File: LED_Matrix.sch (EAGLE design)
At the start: 35 parts, among them IC1 KF33, IC2 FT232RL, Q1 16MHz, U1 HC_05

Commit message: version 1
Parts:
- removed JP2: (no value), pinhead:PINHD-1X2/90
- added C15: 100n, rcl:C-EUC0805
- added C16: 47n, rcl:C-EUC0805
- added C17: 10u, rcl:C-EUC0805
- added C18: 250u, rcl:CPOL-EU153CLV-0605
- added C19: 470n, rcl:C-EUC0805
- added J1: DCJ0202, con-jack:DCJ0202
- added LED3: (no value), led:LEDSML0805
- added LM386: LM386SO08, debegr92:LM386SO08
- added MIC: MIC_EMY-9765PEMY-9765P, debegr92:MIC_EMY-9765PEMY-9765P
- added Q2: (no value), semicon-smd-ipc:NPN-TRANSISTOR_SOT23
- added R6: 10, rcl:R-EU_R0805
- added R7: 10k, rcl:R-EU_R0805
- added R9: 470, rcl:R-EU_R0805
- added TRIMMER: 10k, Tobias:75H_RTRIM
- Q1: device special:XTAL -> crystal:CRYSTALHC49UP
- R8: value 10k -> 470
- renumbered 470 to R8, IC2 to FT232, JP1 to BTM, S2 to RESET, SJ1 to JTX, SJ2 to JRX, U$1 to USB, U1 to HC05
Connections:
- new net BTM_RST: ATMEGA328.PB0(ICP1/CLKO/PCINT0), R7.1
- new net N$16: C19.1, MIC.1, TRIMMER.S
- new net N$17: C17.2, LM386.GAIN2
- new net N$18: C16.2, R6.1
- new net N$2: C15.1, LM386.BYPASS
- new net N$20: C17.1, LM386.GAIN1
- new net N$21: C16.1, C18.+, LM386.OUT
- new net N$22: C19.2, LM386.+
- new net N$23: C9.1, HC05.RST, Q2.C, R5.2
- new net N$24: HC05.PIO1, LED3.A
- new net N$25: LED3.C, R9.2
- net +5V: now also J1.1, LM386.V+, TRIMMER.E; no longer JP2.2
- net AUDIO_IN: now also C18.-
- net GND: now also C15.2, HC05.GND2, J1.2, J1.3, LM386.-, LM386.GND, MIC.2, Q2.E, R6.2, R9.1, TRIMMER.A; no longer JP2.1
- net N$12: now also ATMEGA328.PC3(ADC3/PCINT11)
- net N$15: now also ATMEGA328.PC2(ADC2/PCINT10)
- net N$19: now also Q2.B, R7.2; no longer C9.1, HC05.RST, R5.2
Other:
- note added: "Gain 200"
- moved on the sheet: C1, C10, C2, C8, C9, ISP, MATRIX, R2, R5

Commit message: analog switch added
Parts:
- removed BTM: (no value), jumper:JP2W
- added Q3: (no value), semicon-smd-ipc:NPN-TRANSISTOR_SOT23
- added R10: 1k, rcl:R-EU_R0805
- R7: value 10k -> 1k
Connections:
- removed net N$10: BTM.1, R4.2
- new net N$27: Q3.B, R10.2
- net BTM_MODESELECT: now also Q3.C, R10.1, R4.2; no longer BTM.2
- net GND: now also Q3.E; no longer BTM.3
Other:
- moved on the sheet: R4
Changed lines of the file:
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@@
 <part name="R3" library="rcl" deviceset="R-EU_" device="R0805" value="470"/>
 <part name="GND8" library="supply1" deviceset="GND" device=""/>
-<part name="BTM" library="jumper" deviceset="JP2W" device=""/>
-<part name="GND9" library="supply1" deviceset="GND" device=""/>
 <part name="R4" library="rcl" deviceset="R-EU_" device="R0805" value="10k"/>
 <part name="P+8" library="supply1" deviceset="+5V" device=""/>
@@
 <part name="Q2" library="semicon-smd-ipc" deviceset="NPN-TRANSISTOR_" device="SOT23"/>
 <part name="GND18" library="supply1" deviceset="GND" device=""/>
-<part name="R7" library="rcl" deviceset="R-EU_" device="R0805" value="10k"/>
+<part name="R7" library="rcl" deviceset="R-EU_" device="R0805" value="1k"/>
 <part name="LED3" library="led" deviceset="LED" device="SML0805"/>
 <part name="GND19" library="supply1" deviceset="GND" device=""/>
 <part name="R8" library="rcl" deviceset="R-EU_" device="R0805" value="470"/>
 <part name="R9" library="rcl" deviceset="R-EU_" device="R0805" value="470"/>
+<part name="Q3" library="semicon-smd-ipc" deviceset="NPN-TRANSISTOR_" device="SOT23"/>
+<part name="R10" library="rcl" deviceset="R-EU_" device="R0805" value="1k"/>
+<part name="GND9" library="supply1" deviceset="GND" device=""/>
 </parts>
 <sheets>
@@
 <instance part="R3" gate="G$1" x="121.92" y="45.72" rot="R90"/>
 <instance part="GND8" gate="1" x="121.92" y="30.48"/>
-<instance part="BTM" gate="1" x="137.16" y="55.88" rot="R270"/>
-<instance part="GND9" gate="1" x="129.54" y="48.26"/>
-<instance part="R4" gate="G$1" x="132.08" y="66.04" rot="R270"/>
+<instance part="R4" gate="G$1" x="127" y="63.5" rot="R270"/>
 <instance part="P+8" gate="1" x="187.96" y="132.08"/>
 <instance part="GND10" gate="1" x="187.96" y="66.04"/>
@@
 <instance part="P+6" gate="1" x="185.42" y="58.42"/>
 <instance part="+3V3" gate="G$1" x="231.14" y="58.42"/>
-<instance part="+3V4" gate="G$1" x="132.08" y="76.2"/>
+<instance part="+3V4" gate="G$1" x="127" y="73.66"/>
 <instance part="USB" gate="G$1" x="172.72" y="93.98"/>
 <instance part="P+7" gate="1" x="180.34" y="101.6"/>
@@
 <instance part="R8" gate="G$1" x="116.84" y="43.18" rot="R90"/>
 <instance part="R9" gate="G$1" x="111.76" y="25.4" rot="R90"/>
+<instance part="Q3" gate="G$1" x="129.54" y="48.26" rot="MR0"/>
+<instance part="R10" gate="G$1" x="137.16" y="43.18" rot="R90"/>
+<instance part="GND9" gate="1" x="127" y="38.1"/>
 </instances>
 <busses>
@@
 <junction x="121.92" y="35.56"/>
 <pinref part="R8" gate="G$1" pin="1"/>
-</segment>
-<segment>
-<pinref part="GND9" gate="1" pin="GND"/>
-<pinref part="BTM" gate="1" pin="3"/>
-<wire x1="129.54" y1="50.8" x2="129.54" y2="53.34" width="0.1524" layer="91"/>
-<wire x1="129.54" y1="53.34" x2="134.62" y2="53.34" width="0.1524" layer="91"/>
 </segment>
 <segment>
@@
 <pinref part="R9" gate="G$1" pin="1"/>
 </segment>
+<segment>
+<pinref part="Q3" gate="G$1" pin="E"/>
+<pinref part="GND9" gate="1" pin="GND"/>
+<wire x1="127" y1="43.18" x2="127" y2="40.64" width="0.1524" layer="91"/>
+</segment>
 </net>
 <net name="N$7" class="0">
@@
 <net name="BTM_MODESELECT" class="0">
 <segment>
-<pinref part="BTM" gate="1" pin="2"/>
 <pinref part="HC05" gate="G$1" pin="PIO11"/>
-<wire x1="134.62" y1="55.88" x2="119.38" y2="55.88" width="0.1524" layer="91"/>
-<wire x1="119.38" y1="55.88" x2="96.52" y2="55.88" width="0.1524" layer="91"/>
-<wire x1="119.38" y1="55.88" x2="119.38" y2="63.5" width="0.1524" layer="91"/>
-<wire x1="119.38" y1="63.5" x2="114.3" y2="63.5" width="0.1524" layer="91"/>
-<junction x="119.38" y="55.88"/>
-<label x="114.3" y="63.5" size="1.27" layer="95" rot="R180" xref="yes"/>
+<wire x1="127" y1="55.88" x2="96.52" y2="55.88" width="0.1524" layer="91"/>
+<wire x1="127" y1="53.34" x2="127" y2="55.88" width="0.1524" layer="91"/>
+<pinref part="R4" gate="G$1" pin="2"/>
+<wire x1="127" y1="55.88" x2="127" y2="58.42" width="0.1524" layer="91"/>
+<junction x="127" y="55.88"/>
+<pinref part="Q3" gate="G$1" pin="C"/>
 </segment>
 <segment>
@@
 <label x="111.76" y="83.82" size="1.27" layer="95" xref="yes"/>
 </segment>
-</net>
-<net name="N$10" class="0">
-<segment>
-<pinref part="BTM" gate="1" pin="1"/>
-<wire x1="134.62" y1="58.42" x2="132.08" y2="58.42" width="0.1524" layer="91"/>
-<wire x1="132.08" y1="58.42" x2="132.08" y2="60.96" width="0.1524" layer="91"/>
-<pinref part="R4" gate="G$1" pin="2"/>
+<segment>
+<pinref part="R10" gate="G$1" pin="1"/>
+<wire x1="137.16" y1="38.1" x2="137.16" y2="35.56" width="0.1524" layer="91"/>
+<label x="137.16" y="35.56" size="1.27" layer="95" rot="R270" xref="yes"/>
 </segment>
 </net>
@@
 <segment>
 <pinref part="R4" gate="G$1" pin="1"/>
-<wire x1="132.08" y1="71.12" x2="132.08" y2="73.66" width="0.1524" layer="91"/>
+<wire x1="127" y1="68.58" x2="127" y2="71.12" width="0.1524" layer="91"/>
 <pinref part="+3V4" gate="G$1" pin="+3V3"/>
 </segment>
@@
 </segment>
 </net>
+<net name="N$27" class="0">
+<segment>
+<pinref part="R10" gate="G$1" pin="2"/>
+<pinref part="Q3" gate="G$1" pin="B"/>
+<wire x1="137.16" y1="48.26" x2="132.08" y2="48.26" width="0.1524" layer="91"/>
+</segment>
+</net>

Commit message: return point
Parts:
- removed JRX, JTX: (no value), jumper:SJ2W
- added LEDON: (no value), led:LEDSML0805
- added R11, R12, R13: 470, rcl:R-EU_R0805
- added U$1: DG2016, Tobias:DG2016
- C18: device rcl:CPOL-EU153CLV-0605 -> rcl:CPOL-EUE2.5-7
- MATRIX: device pinhead:PINHD-1X3/90 -> pinhead:PINHD-1X3
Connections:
- new net N$10: LEDON.C, R11.2
- new net N$26: HC05.RX, R12.1, R13.2
- new net N$28: ATMEGA328.PD2(INT0/PCINT18), U$1.IN1
- new net N$29: ATMEGA328.PD3(INT1/OC2B/PCINT19), U$1.IN2
- net +5V: now also LEDON.A, U$1.VCC
- net GND: now also R11.1, R13.1, U$1.GND
- net N$12: now also U$1.COM1; no longer JTX.2
- net N$15: now also U$1.COM2; no longer JRX.2
- net RX_BTM: now also R12.2, U$1.NC1; no longer HC05.RX, JRX.1
- net RX_FT232: now also U$1.NO1; no longer JRX.3
- net TX_BTM: now also U$1.NC2; no longer JTX.1
- net TX_FT232: now also U$1.NO2; no longer JTX.3

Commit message: version 2 Final
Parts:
- removed C15: 100n, rcl:C-EUC0805
- removed C16: 47n, rcl:C-EUC0805
- removed C17: 10u, rcl:C-EUC0805
- removed C18: 250u, rcl:CPOL-EUE2.5-7
- removed C19: 470n, rcl:C-EUC0805
- removed C4, C5: 22p, rcl:C-EUC0805
- removed LM386: LM386SO08, debegr92:LM386SO08
- removed MIC: MIC_EMY-9765PEMY-9765P, debegr92:MIC_EMY-9765PEMY-9765P
- removed Q1: 16MHz, crystal:CRYSTALHC49UP
- removed R6: 10, rcl:R-EU_R0805
- removed TRIMMER: 10k, Tobias:75H_RTRIM
- added Q4: CSTCR6M00G53Z, murata-filter:CSTCR6M00G53Z
- added SJ1: (no value), jumper:SJ
- renumbered IC1 to KF33, LEDON to D1, MATRIX to MTX, U$1 to DG2016
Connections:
- removed net N$16: C19.1, MIC.1, TRIMMER.S
- removed net N$17: C17.2, LM386.GAIN2
- removed net N$18: C16.2, R6.1
- removed net N$20: C17.1, LM386.GAIN1
- removed net N$21: C16.1, C18.+, LM386.OUT
- removed net N$22: C19.2, LM386.+
- net +5V: now also SJ1.2; no longer LM386.V+, TRIMMER.E, USB.VCC
- net AUDIO_IN: no longer C18.-
- net GND: now also Q4.2; no longer C15.2, C4.1, C5.1, LM386.-, LM386.GND, MIC.2, R6.2, TRIMMER.A
- net N$2: now also SJ1.1, USB.VCC; no longer C15.1, LM386.BYPASS
- net N$3: now also Q4.1; no longer C4.2, Q1.1
- net N$7: now also Q4.3; no longer C5.2, Q1.2
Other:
- note removed: "Gain 200"

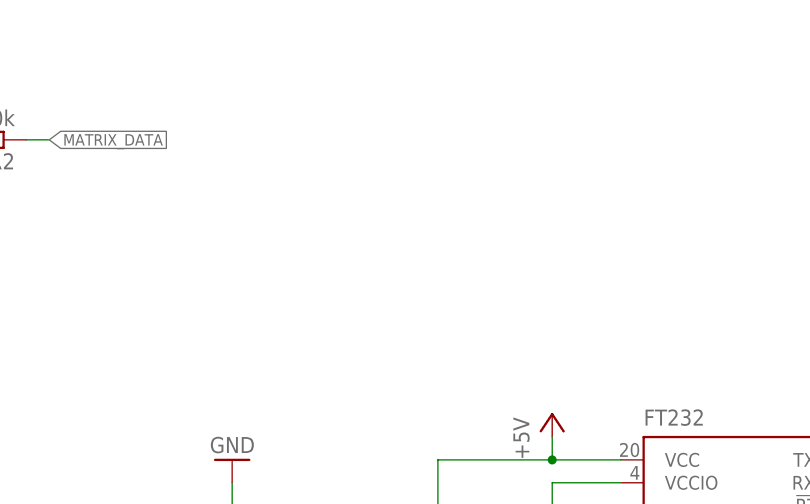
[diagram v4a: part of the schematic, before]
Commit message: Audo in added
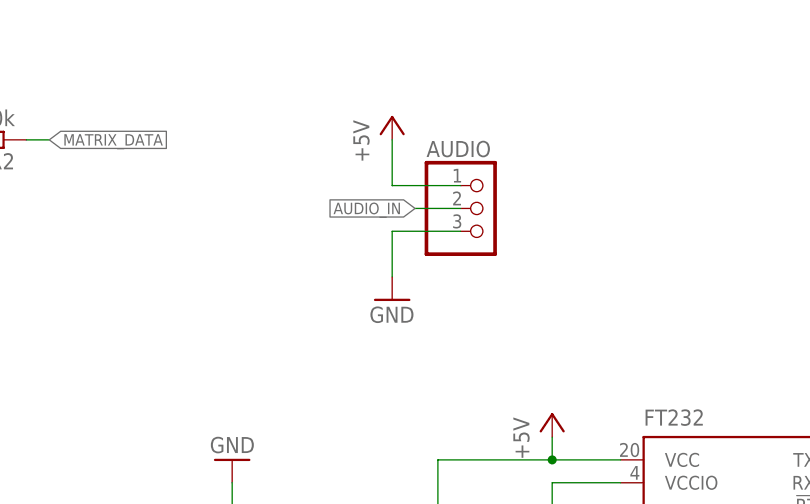
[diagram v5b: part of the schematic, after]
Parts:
- added AUDIO: (no value), pinhead:PINHD-1X3
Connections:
- net +5V: now also AUDIO.1
- net AUDIO_IN: now also AUDIO.2
- net GND: now also AUDIO.3
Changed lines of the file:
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@@
 <part name="SJ1" library="jumper" deviceset="SJ" device=""/>
 <part name="Q4" library="murata-filter" deviceset="CSTCR" device="" technology="6M00G53Z"/>
+<part name="AUDIO" library="pinhead" deviceset="PINHD-1X3" device=""/>
+<part name="P+9" library="supply1" deviceset="+5V" device=""/>
+<part name="GND15" library="supply1" deviceset="GND" device=""/>
 </parts>
 <sheets>
@@
 <instance part="SJ1" gate="1" x="182.88" y="101.6" rot="R90"/>
 <instance part="Q4" gate="G$1" x="30.48" y="109.22" rot="R270"/>
+<instance part="AUDIO" gate="A" x="180.34" y="154.94"/>
+<instance part="P+9" gate="1" x="170.18" y="165.1"/>
+<instance part="GND15" gate="1" x="170.18" y="144.78"/>
 </instances>
 <busses>
@@
 <pinref part="P+7" gate="1" pin="+5V"/>
 <wire x1="182.88" y1="109.22" x2="182.88" y2="106.68" width="0.1524" layer="91"/>
+</segment>
+<segment>
+<pinref part="AUDIO" gate="A" pin="1"/>
+<wire x1="177.8" y1="157.48" x2="170.18" y2="157.48" width="0.1524" layer="91"/>
+<pinref part="P+9" gate="1" pin="+5V"/>
+<wire x1="170.18" y1="162.56" x2="170.18" y2="157.48" width="0.1524" layer="91"/>
 </segment>
 </net>
@@
 <pinref part="GND22" gate="1" pin="GND"/>
 </segment>
+<segment>
+<pinref part="AUDIO" gate="A" pin="3"/>
+<wire x1="177.8" y1="152.4" x2="170.18" y2="152.4" width="0.1524" layer="91"/>
+<pinref part="GND15" gate="1" pin="GND"/>
+<wire x1="170.18" y1="147.32" x2="170.18" y2="152.4" width="0.1524" layer="91"/>
+</segment>
 </net>
 <net name="N$7" class="0">
@@
 <label x="114.3" y="132.08" size="1.27" layer="95" xref="yes"/>
 </segment>
-</net>
+<segment>
+<pinref part="AUDIO" gate="A" pin="2"/>
+<wire x1="177.8" y1="154.94" x2="172.72" y2="154.94" width="0.1524" layer="91"/>
+<label x="172.72" y="154.94" size="1.27" layer="95" rot="R180" xref="yes"/>
+</segment>
+</net>
